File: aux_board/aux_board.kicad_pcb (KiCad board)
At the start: 4 copper layers, 80 x 80 mm, 108 parts, among them J1 Conn_02x13_Odd_Even, J2 Conn_02x05_Odd_Even, J3 Conn_01x02_Pin, J4 PC104 Conn_02x20_Odd_Even, J5 Conn_01x03_Pin, J6 Conn_01x03_Pin, J7 10155435-00011LF, J8 10155435-00011LF, J9 10155435-00011LF, SW1 EVP-AA602W, SW2 EVP-AA602W, U1 STM32L496RGTx, U2 TCAN3414, U3 TCAN3414, U4 FT230XS, U5 FT230XS, U6 TPS631000DRLR, U7 TPS631000DRLR, U8 TPS631000DRLR, X1 10MHz

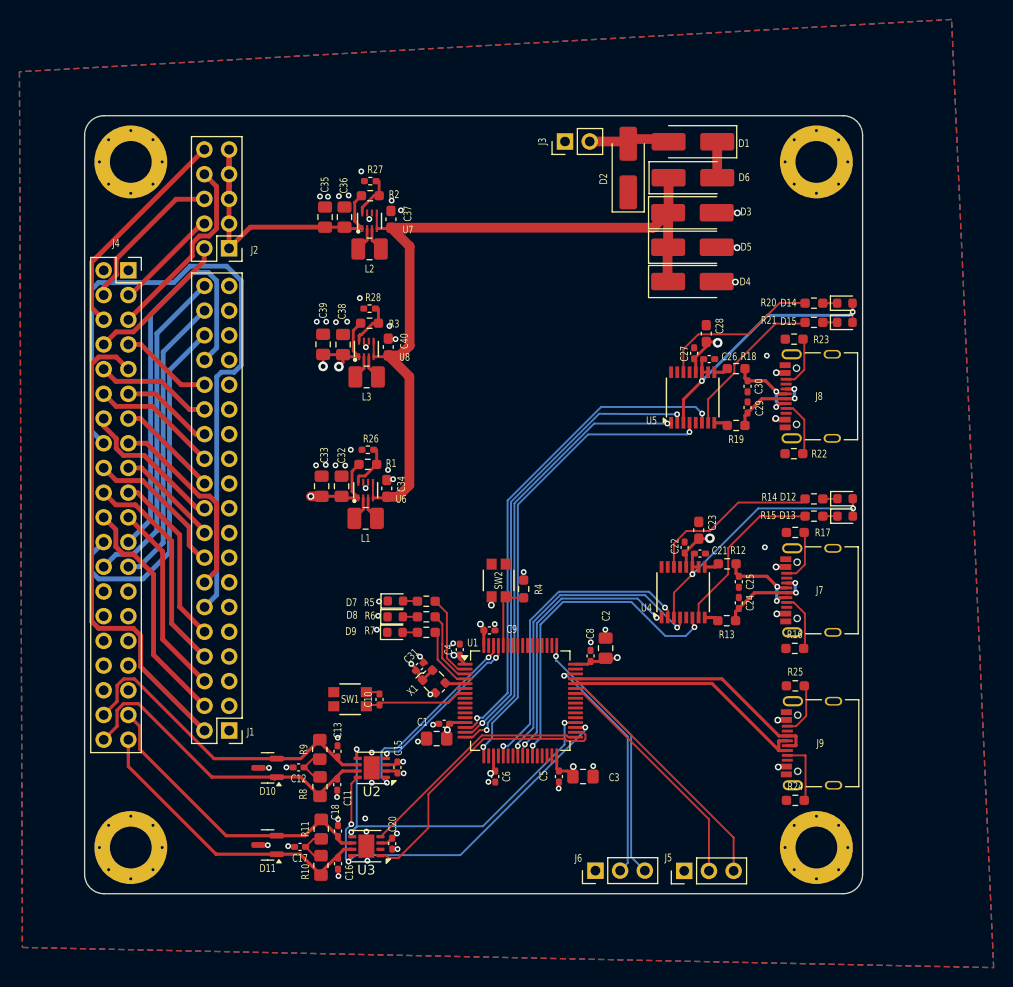
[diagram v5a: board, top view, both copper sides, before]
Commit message: create and check BOM, check MC pinout, CAN standby and shutdown for each channel
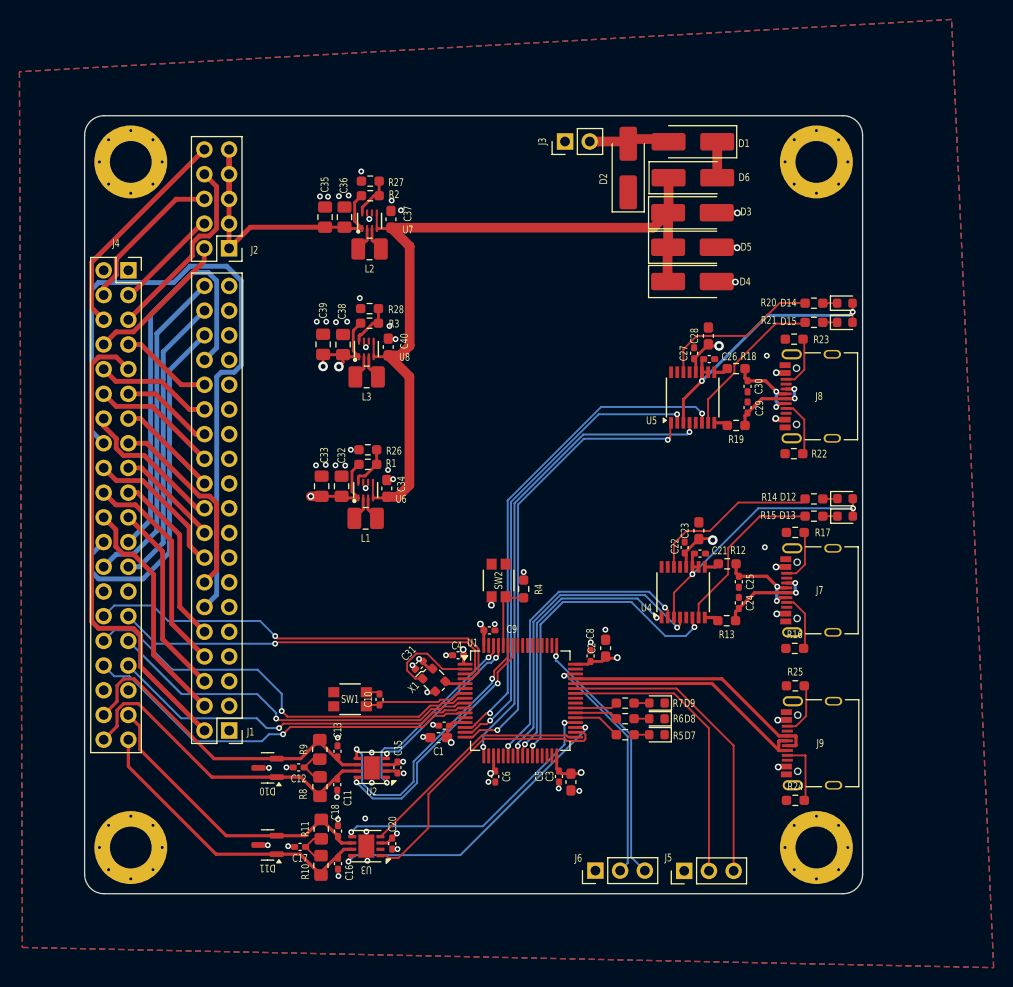
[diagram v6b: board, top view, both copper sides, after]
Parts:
- C1, C2, C3: value 10u -> 10uF; footprint Capacitor_SMD:C_0805_2012Metric_Pad1.18x1.45mm_HandSolder -> Capacitor_SMD:C_0603_1608Metric_Pad1.08x0.95mm_HandSolder
- C10, C15, C20, C21, C22, C26, C27, C31, C4, C5, C6, C7, C8, C9: value 100n -> 100nF
- C11, C13, C16, C18: value 100p -> 100pF
- C12, C17: value 4.7n -> 4.7nF
- C23, C28: value 1u -> 10uF
- D10, D11: value NUP2105L -> NUP2105LT1G
- D2: value SMAJ6.0CA -> SMAJ5.0A
- J1: value Conn_02x13_Odd_Even -> Conn_02x19_Odd_Even
- L1, L2, L3: value 1u -> 1uH
- R14, R15, R20, R21: value 680R -> 1K
- R2: value 673K4 -> 673K
- R26, R27, R28: footprint Resistor_SMD:R_0402_1005Metric_Pad0.72x0.64mm_HandSolder -> Resistor_SMD:R_0603_1608Metric_Pad0.98x0.95mm_HandSolder
- R5, R6, R7: value 680 -> 1K
- U1: value STM32L496RGTx -> STM32L496RGT6
- moved D7 30.2 mm to (118.8, 123.7), turned to 180 degrees
- moved D8 28.9 mm to (118.8, 122.0), turned to 180 degrees
- moved D9 27.9 mm to (118.9, 120.4), turned to 180 degrees
- moved R5 24.6 mm to (115.6, 123.7), turned to 0 degrees
- moved R6 23.0 mm to (115.6, 122.0), turned to 0 degrees
- moved R7 21.7 mm to (115.6, 120.4), turned to 0 degrees
- moved C3 1.36 mm to (110.0, 128.5), turned to -90 degrees
- moved C4 0.61 mm to (98.4, 115.5), turned to 180 degrees
- moved C28 0.32 mm to (124.1, 82.6)
- moved C1 0.22 mm to (96.4, 124.0)
- moved C7 0.20 mm to (97.0, 122.7)
- moved X1 0.16 mm to (95.9, 118.0)
- moved C31 0.13 mm to (94.4, 116.5), turned to -135 degrees
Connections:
- J4 pad 29: /INTERBOARD_CONNECTOR/*ATTENTION -> /*ATTENTION
- J4 pad 30: /INTERBOARD_CONNECTOR/*EPS_RST -> /*EPS_RST
- J4 pad 31: /INTERBOARD_CONNECTOR/*SCI_RST -> /*SCI_RST
- J4 pad 32: /INTERBOARD_CONNECTOR/*AVI_RST -> /*AVI_RST
- J4 pad 33: /INTERBOARD_CONNECTOR/*COMM1_RST -> /*COMM1_RST
- J4 pad 34: /INTERBOARD_CONNECTOR/*COMM2_RST -> /*COMM2_RST
- R5 pad 1: Net-(U1-PC13) -> Net-(U1-PC6)
- R6 pad 1: Net-(U1-PC14) -> Net-(U1-PC7)
- R7 pad 1: Net-(U1-PC15) -> Net-(U1-PC8)
- U1 pad 10: unconnected-(U1-PC2-Pad10) -> /*COMM1_RST
- U1 pad 11: unconnected-(U1-PC3-Pad11) -> /*COMM2_RST
- U1 pad 2: Net-(U1-PC13) -> /CAN TO USB/OSC_HSE_OE
- U1 pad 21: /CAN TO USB/USART3_CTS -> unconnected-(U1-PA5-Pad21)
- U1 pad 22: unconnected-(U1-PA6-Pad22) -> /CAN TO USB/USART3_CTS
- U1 pad 3: Net-(U1-PC14) -> /*ATTENTION
- U1 pad 35: /CAN TO USB/CAN_STB -> /CAN TO USB/CAN2_STB
- U1 pad 36: /CAN TO USB/CAN_SHTD -> /CAN TO USB/CAN2_SHTD
- U1 pad 37: unconnected-(U1-PC6-Pad37) -> Net-(U1-PC6)
- U1 pad 38: unconnected-(U1-PC7-Pad38) -> Net-(U1-PC7)
- U1 pad 39: unconnected-(U1-PC8-Pad39) -> Net-(U1-PC8)
- U1 pad 4: Net-(U1-PC15) -> /*EPS_RST
- U1 pad 58: unconnected-(U1-PB6-Pad58) -> /CAN TO USB/CAN1_STB
- U1 pad 59: unconnected-(U1-PB7-Pad59) -> /CAN TO USB/CAN1_SHTD
- U1 pad 8: unconnected-(U1-PC0-Pad8) -> /*AVI_RST
- U1 pad 9: unconnected-(U1-PC1-Pad9) -> /*SCI_RST
- U2 pad 5: /CAN TO USB/CAN_SHTD -> /CAN TO USB/CAN1_SHTD
- U2 pad 8: /CAN TO USB/CAN_STB -> /CAN TO USB/CAN1_STB
- U3 pad 5: /CAN TO USB/CAN_SHTD -> /CAN TO USB/CAN2_SHTD
- U3 pad 8: /CAN TO USB/CAN_STB -> /CAN TO USB/CAN2_STB
- X1 pad 1: +3V3 -> /CAN TO USB/OSC_HSE_OE
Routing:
- net /*EPS_RST: track 0.00 -> 44.9 mm, vias 0 -> 1
- net /*AVI_RST: track 0.00 -> 43.1 mm, vias 0 -> 1
- net /*COMM2_RST: track 0.00 -> 41.6 mm, vias 0 -> 1
- net /CAN TO USB/CAN_STB: track 41.3 -> 0.00 mm, vias 3 -> 0
- net /*ATTENTION: track 0.00 -> 40.5 mm, vias 0 -> 1
- net /*SCI_RST: track 0.00 -> 39.5 mm, vias 0 -> 1
- net /CAN TO USB/CAN_SHTD: track 39.2 -> 0.00 mm, vias 3 -> 0
- net /*COMM1_RST: track 0.00 -> 38.1 mm, vias 0 -> 1
- net /CAN TO USB/CAN2_STB: track 0.00 -> 32.0 mm, vias 0 -> 2
- net /CAN TO USB/CAN2_SHTD: track 0.00 -> 29.5 mm, vias 0 -> 2
- net /CAN TO USB/CAN1_SHTD: track 0.00 -> 29.1 mm, vias 0 -> 2
- net /CAN TO USB/CAN1_STB: track 0.00 -> 26.4 mm, vias 0 -> 2
- net /CAN TO USB/OSC_HSE_OE: track 0.00 -> 9.75 mm
- net Net-(U1-PC13): track 8.68 -> 0.00 mm
- net Net-(U1-PC14): track 7.59 -> 0.00 mm
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
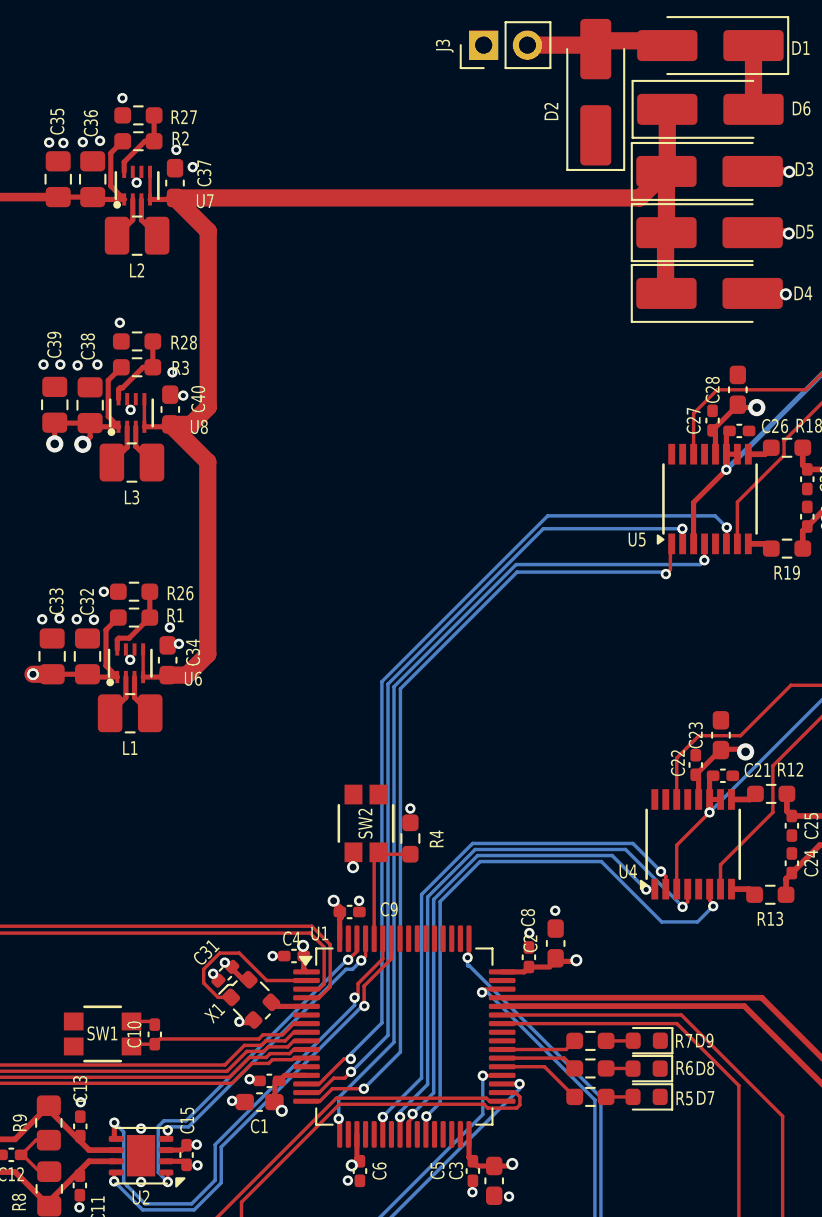
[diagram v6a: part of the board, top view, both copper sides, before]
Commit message: reduce some R to 0402 for consistency with imported components
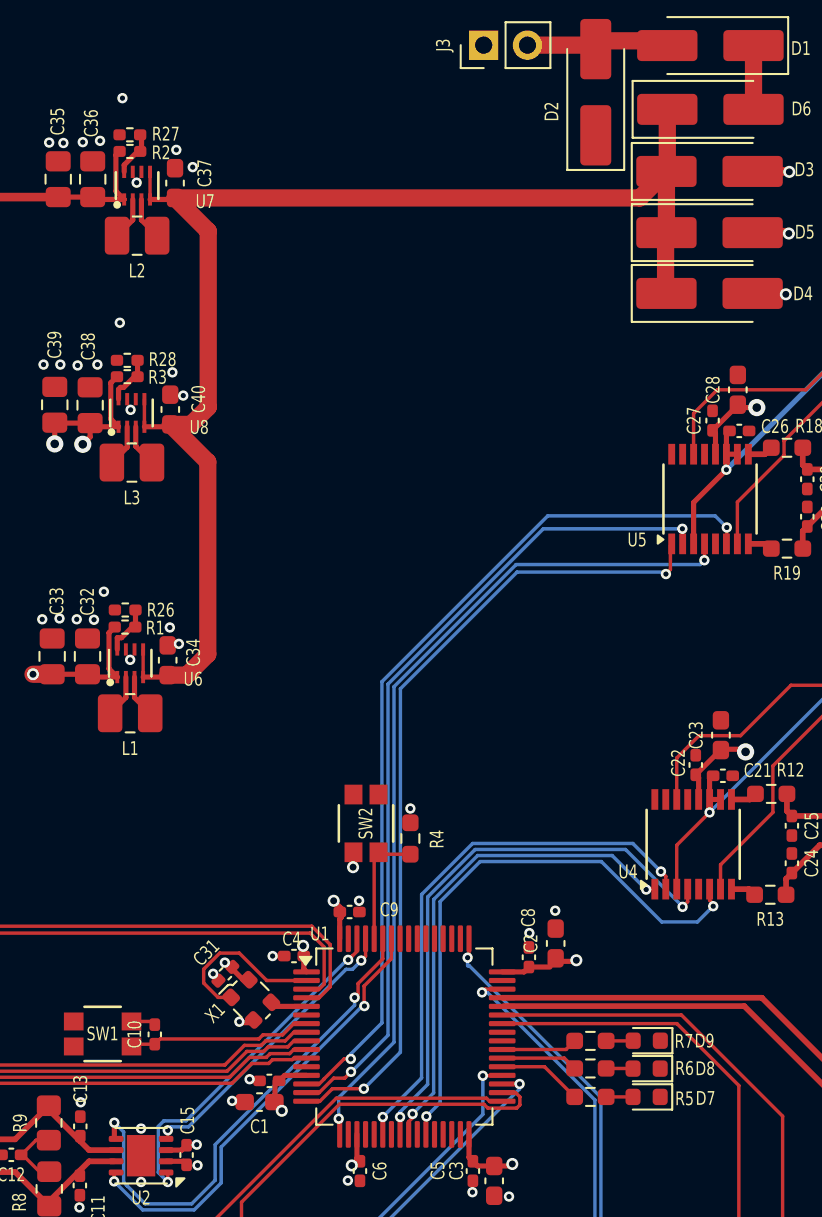
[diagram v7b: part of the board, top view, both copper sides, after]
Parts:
- C32, C33, C35, C36, C38, C39: value 47u -> 47uF
- C34, C37, C40: value 22u -> 22uF
- R1, R2, R26, R27, R28, R3: footprint Resistor_SMD:R_0603_1608Metric_Pad0.98x0.95mm_HandSolder -> Resistor_SMD:R_0402_1005Metric_Pad0.72x0.64mm_HandSolder
- moved R28 1.24 mm to (88.7, 80.9)
- moved R27 1.23 mm to (88.9, 67.8)
- moved R26 1.18 mm to (88.6, 95.4)
- moved R3 0.79 mm to (88.7, 81.9)
- moved R2 0.77 mm to (88.9, 68.8)
- moved R1 0.76 mm to (88.6, 96.4)
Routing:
- net /Regulator 4V2/R-: track 4.31 -> 2.38 mm
- net /Regulator 3V3/R-: track 4.59 -> 2.82 mm
- net /Regulator 5V/R-: track 4.49 -> 2.87 mm
- net +VBAT: track 36.2 -> 35.3 mm
- net +5V: track 93.3 -> 92.5 mm
- net +3V3: track 42.6 -> 41.9 mm
